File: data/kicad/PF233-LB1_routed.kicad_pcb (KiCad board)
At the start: 4 copper layers, 78 x 77.2 mm, 81 parts, among them U1 74AHCT1G125

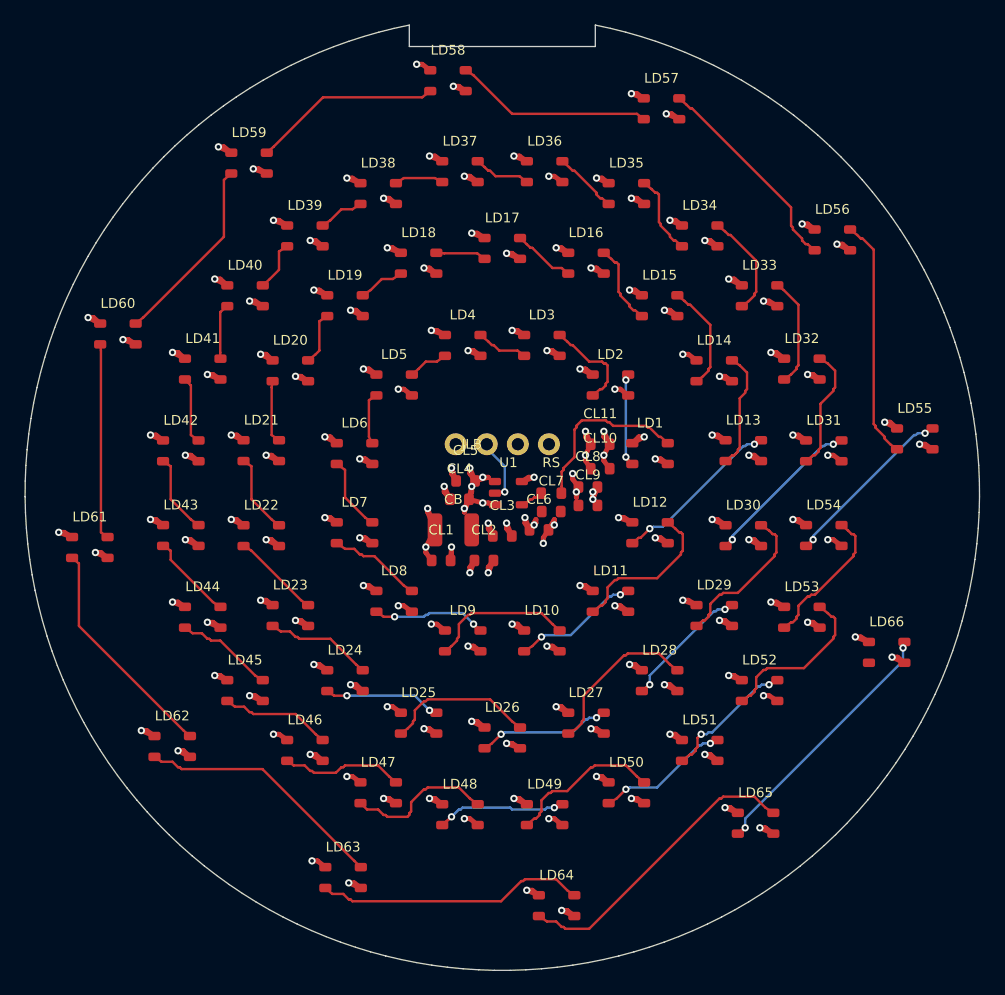
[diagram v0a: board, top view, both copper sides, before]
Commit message: External KiCad 9 DRC, CB1D-B revision, HV plane keep-out, router/export fixes (step 1 of the transmit-region sign-off)
- KiCad 9.0.9 installed; kicad_drc.py (zone fill, design rules, automatic negative control), dru_gen.py (last rule wins), make kicad-drc
- CB1D-B: MONO 460 V tap and joystick inputs removed, parts kept inside the rib annulus; 58 parts, 41/41 nets, 1669 mm, 101 vias
- CB1D and LB1: KiCad 0 errors / 0 unconnected; independent DRC 0/0; head cross-check 0 fail; wiring audit clean
- gerber_out: 1.0 mm plane keep-out for HV pads and vias (gerber_hv_check.py, control proves the old writer failed 8/8)
- route_fix: nearest-pad stubs, circle test for round pads, duplicate vias; kicad_inject: template zones no longer kept
- new Gerbers CB1D_B and LB1_v4; CB1D_v2 and LB1_v3_stubbed marked superseded
- regress 39 pass; CORRECTIONS, DESIGN_STATE, OPEN_ITEMS 20/23/24, ASSUMPTIONS 30

Not done: PB1R routing, TXJ1 edge clearance, SB1R annular rings, CAM viewer, datasheets, bench test.

Co-Authored-By: Claude Sonnet 5.5 <noreply@anthropic.com>
Claude-Session: https://claude.ai/code/session_01T7iU5pGiBfkKRBbe2JcTJx
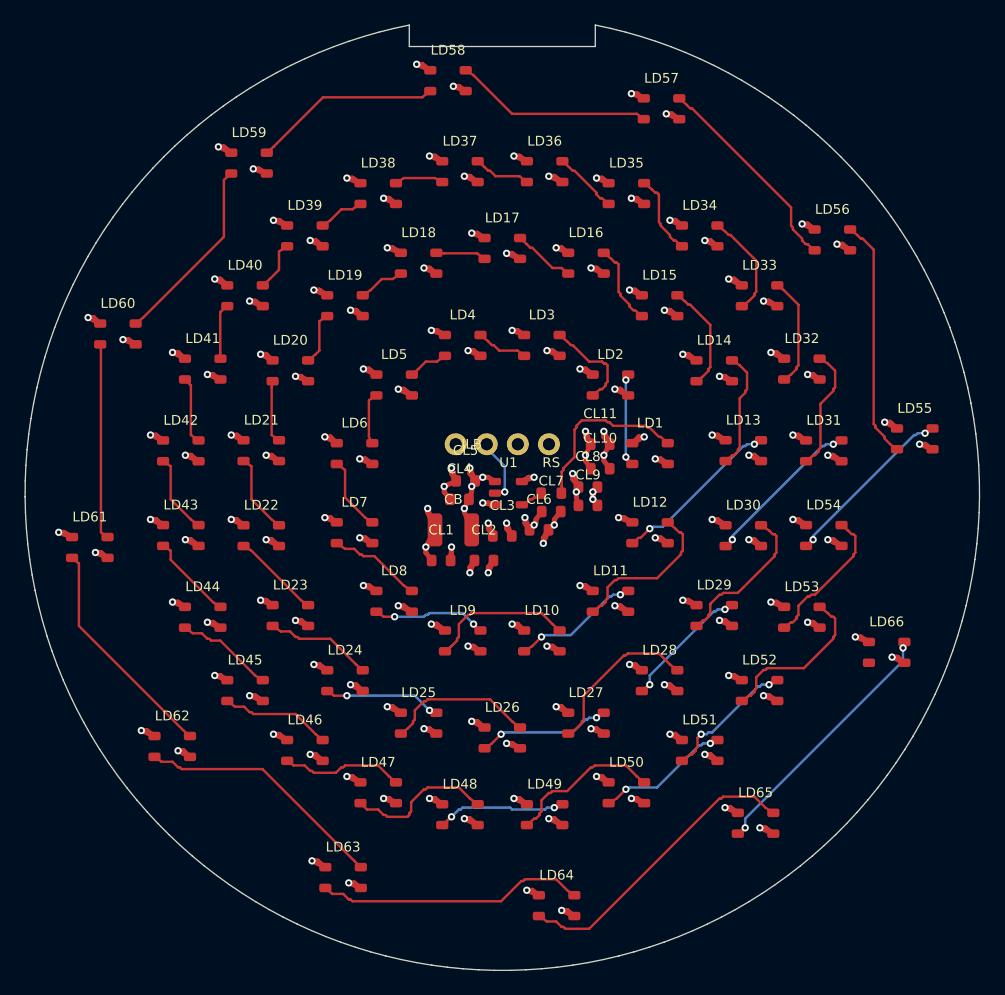
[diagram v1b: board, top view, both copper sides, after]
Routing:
- net GND: track 173.2 -> 183.3 mm
- net +5V: track 174.6 -> 183.9 mm
- net LED_IN: track 5.20 -> 6.06 mm
